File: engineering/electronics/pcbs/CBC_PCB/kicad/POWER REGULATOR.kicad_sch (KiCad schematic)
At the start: 109 parts, among them U601 MP9486GN-Z, U602 MP9486GN-Z, U603 1uF, U605 120pF, U606 10mΩ, U607 MAX40203AUK+T, U608 MAX40203AUK+T, U609 1uH, U613 MAX40203AUK+T, U614 MAX40203AUK+T

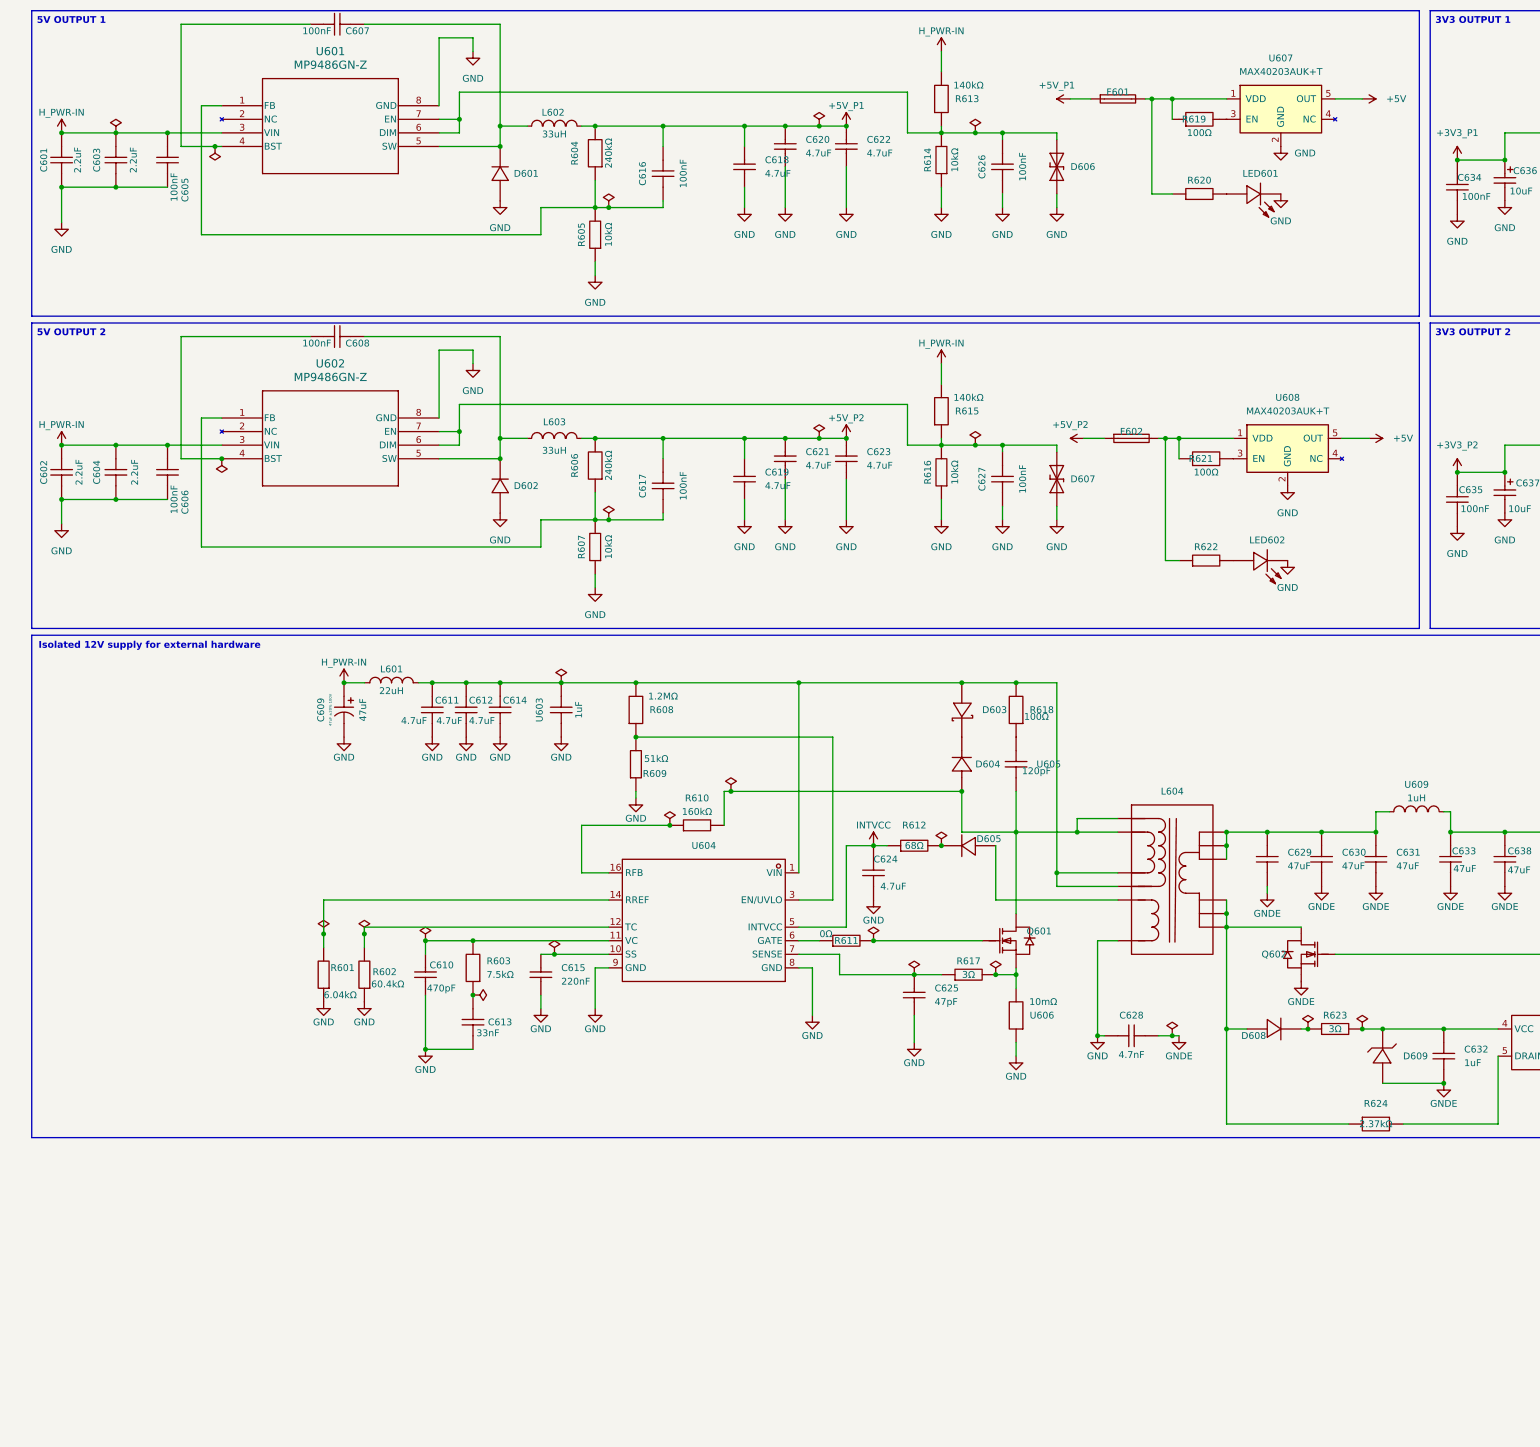
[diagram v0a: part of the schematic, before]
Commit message: feat(cbc): integrate PT1.5 CBC PCB update for the US build
Julius's CPC_PCB_21_10_26_5 package (issue #58): precharge ground fix with the new H_PWR-OUT- net and NT201, precharge and HV bus sensing, BZ501 buzzer, aux input inrush limiting (RT601, R628/R629, F604), BOM-review part swaps, and JLC production outputs. The board STEP is zipped because the raw export is 127 MB, which is over GitHub's 100 MB file limit.
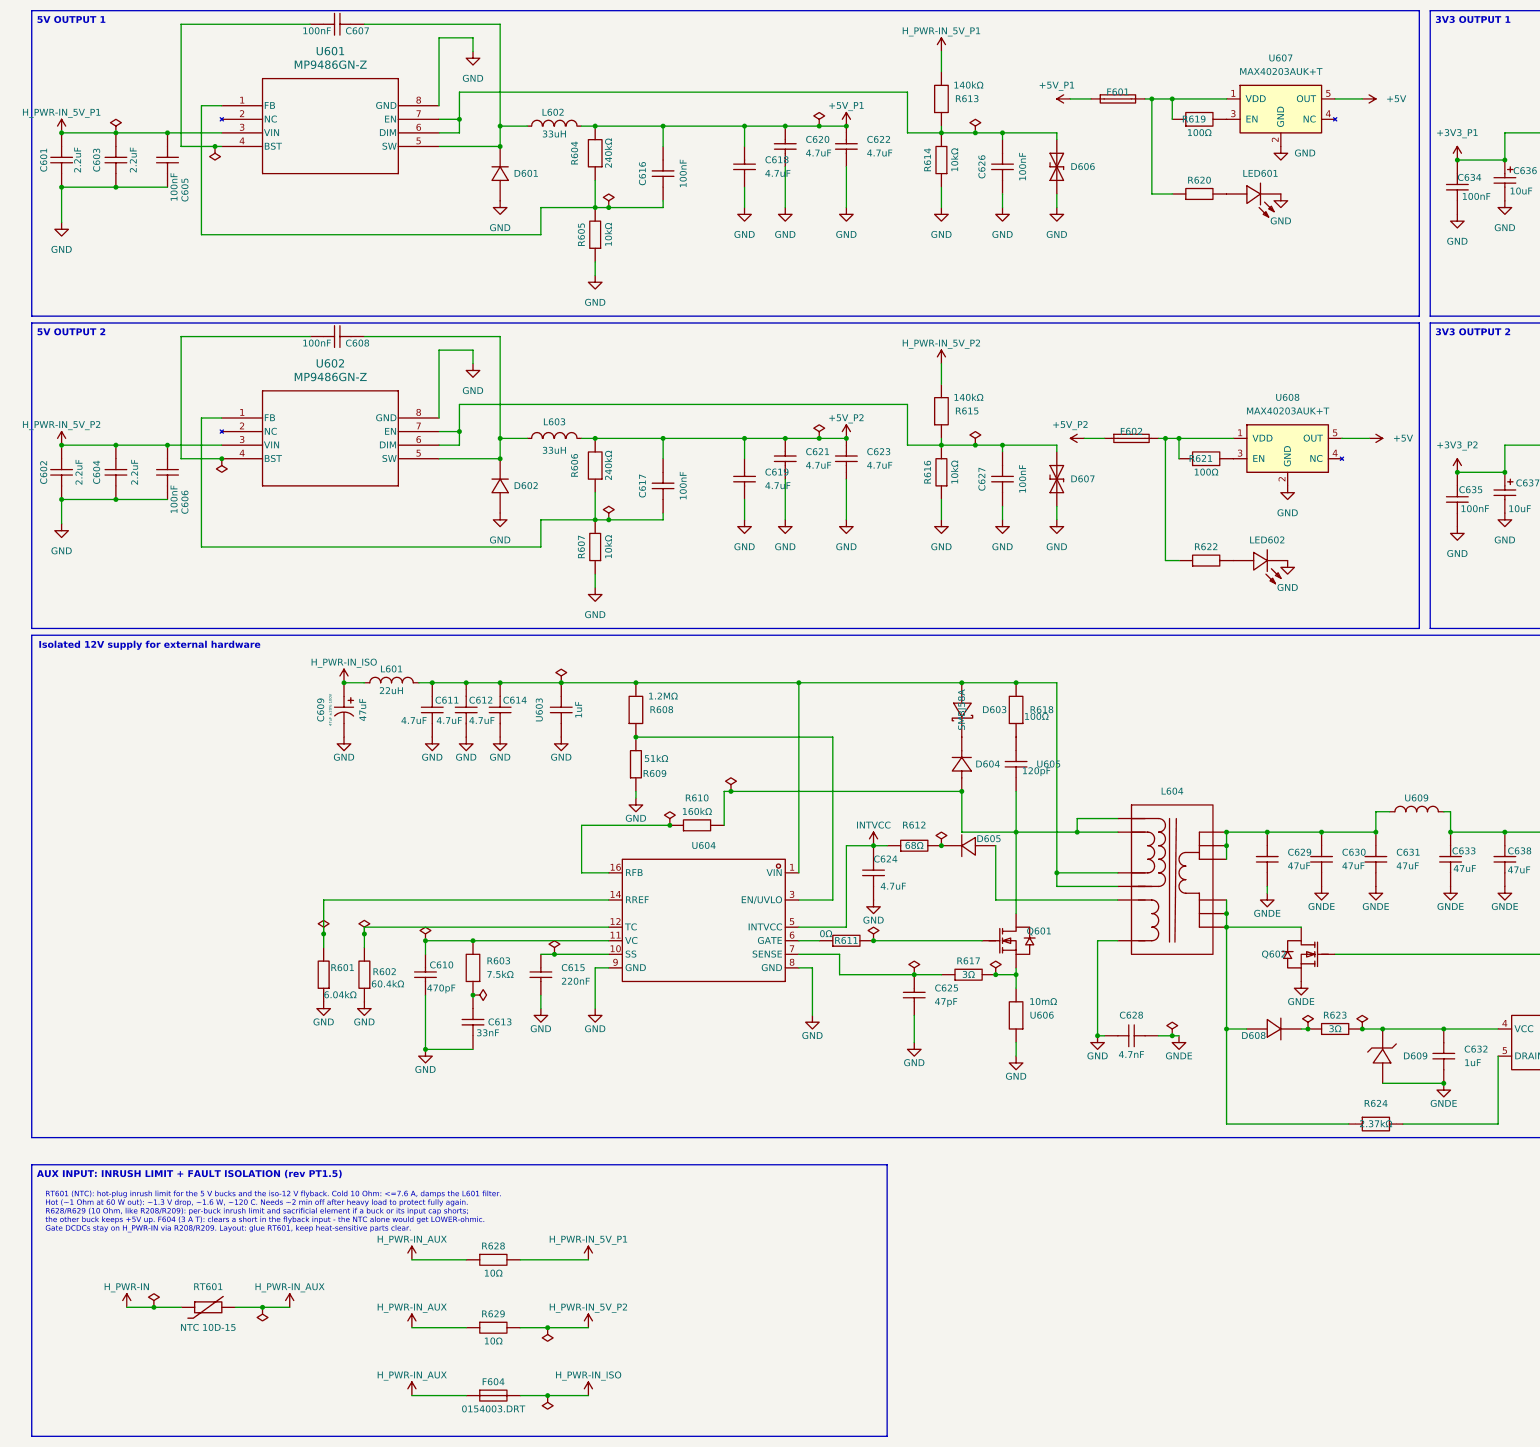
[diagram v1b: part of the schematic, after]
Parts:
- added F604: 0154003.DRT, EasyEDA_Lib:FUSE-SMD_L9.8-W5.1, symbol CBC_PCB:0154005.DR
- added R628, R629: 10Ω, EasyEDA_Lib:R2512, symbol CBC_PCB:25121WF100JT4E
- added RT601: NTC 10D-15, EasyEDA_Lib_2:RES-TH_L12.5-W5.1-P7.50-D1.2-S2.20, symbol CBC_PCB:NTC_10D-15
- C625: Manufacturer SAMSUNG(三星) -> muRata; Manufacturer Part CL10C470JB8NNNC -> GCM1885C2A470JA16D; Supplier Part C1671 -> C126580
- D603: value (none) -> SMBJ58A; LCSC Part Name SMBJ85A-13-F -> SMBJ58A; Manufacturer DIODES(美台) -> Littelfuse; Manufacturer Part SMBJ85A-13-F -> SMBJ58A; Supplier Part C135108 -> C157526
- D604: Manufacturer Central(中环) -> DOWO; Manufacturer Part CMMR1U-02 TR PBFREE -> ES1DFL; Supplier Part C5354735 -> C48996687
- R611: Manufacturer YAGEO(国巨) -> UNI-ROYAL; Manufacturer Part RC0402FR-070RL -> 0402WGF0000TCE; Supplier Part C106231 -> C17168
- R618: footprint EasyEDA_Lib:R0603 -> Resistor_SMD:R_2010_5025Metric; LCSC Part Name 薄膜电阻 100Ω ±0.1% 100mW -> 100Ω ±1% 750mW 2010; Manufacturer RESI(开步睿思) -> UNI-ROYAL; Manufacturer Part PTFR0603B100RN9 -> 201007F1000T4E; Supplier Part C394538 -> C421954
- U601, U602: Manufacturer (none) -> MPS; Manufacturer Part (none) -> MP9486GN-Z; Supplier (none) -> LCSC; Supplier Part (none) -> C6675210
- U604: Manufacturer ADI(亚德诺) -> ADI; Manufacturer Part LT3748EMS#PBF -> LT3748HMS#PBF; Supplier Part C117158 -> C580126
- U605: footprint EasyEDA_Lib:C0603 -> EasyEDA_Lib:C0805; LCSC Part Name 120pF ±1% 100V -> 120pF ±5% 500V NP0; Manufacturer muRata(村田) -> YAGEO; Manufacturer Part GCM1885C2A121FA16D -> CC0805JRNPOBBN121; Supplier Part C1864338 -> C527211
- U609: value 1uH -> (none); footprint EasyEDA_Lib:IND-SMD_L6.6-W6.4_XAL6060-103ME -> EasyEDA_Lib_2:IND-SMD_L7.0-W6.6; symbol CBC_PCB:XAL6030-102MEC -> EasyEDA_Lib_2:FAUL0630-1R0MT; LCSC Part Name 1uH ±20% 23A -> 1uH ±20% 15A; Manufacturer Coilcraft(线艺) -> cjiang(长江微电); Manufacturer Part XAL6030-102MEC -> FAUL0630-1R0MT; Supplier Part C2938919 -> C3040349
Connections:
- net H_PWR-IN: now also RT601.1; no longer C601.2, C602.2, C603.2, C604.2, C605.1, C606.1, C609.1, L601.1, R613.2, R615.2, U601.3 (VIN), U602.3 (VIN)
- new net H_PWR-IN_5V_P1: C601.2, C603.2, C605.1, R613.2, R628.2, U601.3 (VIN)
- new net H_PWR-IN_5V_P2: C602.2, C604.2, C606.1, R615.2, R629.2, U602.3 (VIN)
- new net H_PWR-IN_AUX: F604.1, R628.1, R629.1, RT601.2
- new net H_PWR-IN_ISO: C609.1, F604.2, L601.1
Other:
- note added: "RT601 (NTC): hot-plug inrush limit for the 5 V bucks and the iso-12 V flyback. Cold 10 Ohm: <=7.6 A, damps the L601 filter. Hot (~1 Ohm at 60 W out): ~1.3 V drop, ~1.6 W, ~120 C. Needs ~2 min off after heavy load to protect fully again. R628/R629 (10 Ohm, like R208/R209): per-buck inrush limit and sacrificial element if a buck or its input cap shorts; the other buck keeps +5V up. F604 (3 A T): cl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"
